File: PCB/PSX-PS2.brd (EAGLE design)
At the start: 58.5 x 61 mm, 15 parts

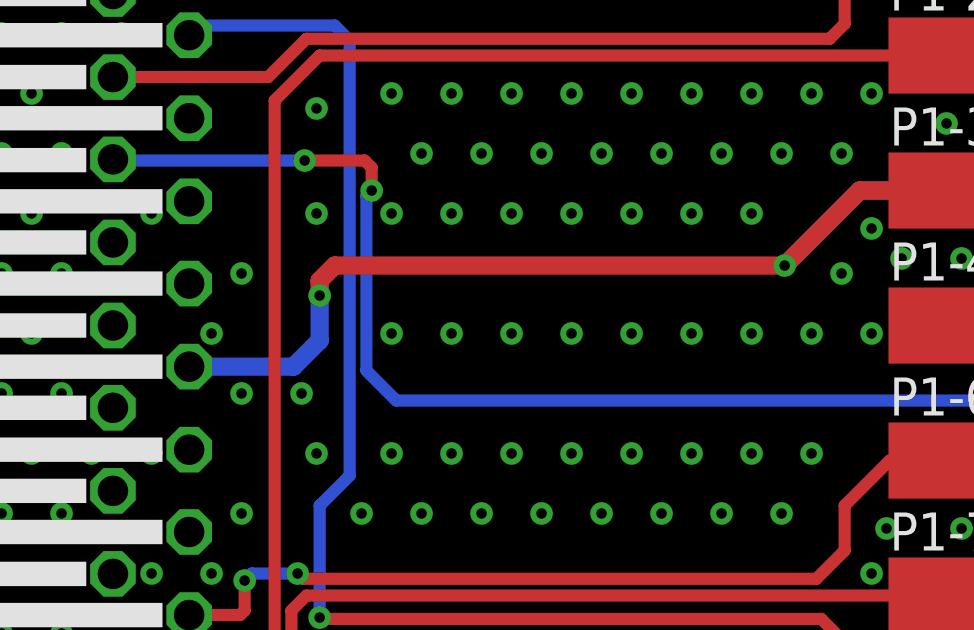
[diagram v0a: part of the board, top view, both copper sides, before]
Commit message: PS2 Power Pin Swap
The PCB could not detect the correct system using the 8V from the PS2 to the 5VIN on the ESP.  Moving to the 3V3 from the PS2 to 3V3IN on the ESP corrected the issue and the PCB not works as intended.
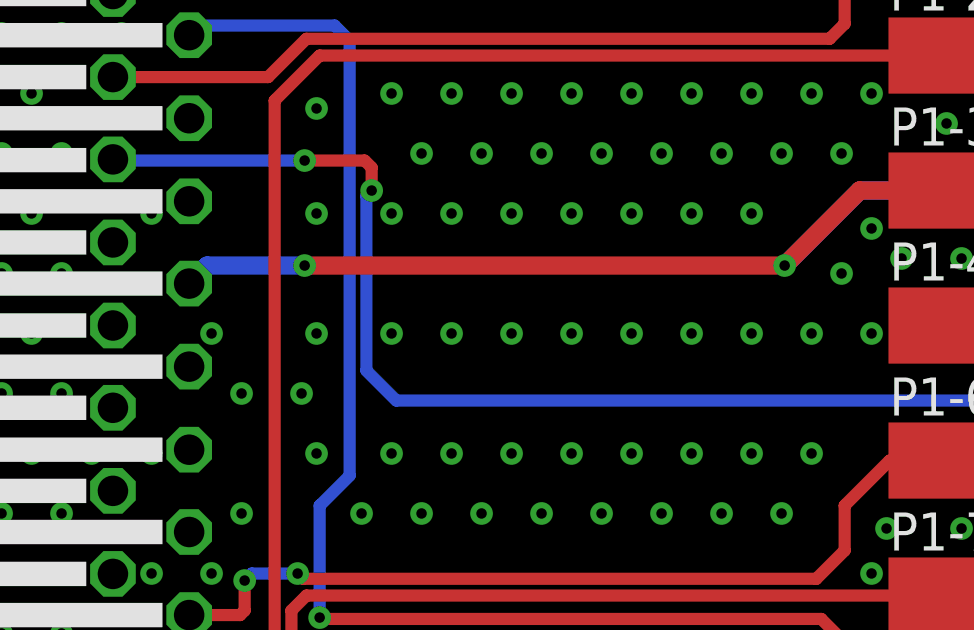
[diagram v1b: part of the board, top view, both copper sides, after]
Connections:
- removed net 5VIN: P1-3.1, P2-3.1, X1.7
- new net 3V3IN: P1-3.1, P2-3.1, X1.8
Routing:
- net 5VIN: track 42.5 -> 0.00 mm, vias 2 -> 0
- net 3V3IN: track 0.00 -> 40.2 mm, vias 0 -> 2
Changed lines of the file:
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@@
 <via x="14.8968" y="29.735840625" extent="1-16" drill="0.35"/>
 <via x="13.8968" y="31.735840625" extent="1-16" drill="0.35"/>
-<via x="14.8968" y="33.735840625" extent="1-16" drill="0.35"/>
+<via x="17.3968" y="31.735840625" extent="1-16" drill="0.35"/>
 <via x="14.8968" y="49.735840625" extent="1-16" drill="0.35"/>
 <via x="13.8968" y="51.735840625" extent="1-16" drill="0.35"/>
@@
 <via x="56.8968" y="45.735840625" extent="1-16" drill="0.35"/>
 </signal>
-<signal name="5VIN">
-<contactref element="X1" pad="7"/>
-<contactref element="P1-3" pad="1"/>
-<contactref element="P2-3" pad="1"/>
-<wire x1="13.15" y1="30.63" x2="16.63" y2="30.63" width="0.6096" layer="16"/>
-<wire x1="16.63" y1="30.63" x2="17.5" y2="31.5" width="0.6096" layer="16"/>
-<wire x1="17.5" y1="31.5" x2="17.5" y2="33" width="0.6096" layer="16"/>
-<via x="17.5" y="33" extent="1-16" drill="0.35"/>
-<wire x1="17.5" y1="33" x2="17.5" y2="33.5" width="0.6096" layer="1"/>
-<wire x1="17.5" y1="33.5" x2="18" y2="34" width="0.6096" layer="1"/>
-<wire x1="35.5" y1="36.5" x2="39" y2="36.5" width="0.6096" layer="1"/>
-<wire x1="18" y1="34" x2="33" y2="34" width="0.6096" layer="1"/>
-<wire x1="33" y1="34" x2="35.5" y2="36.5" width="0.6096" layer="1"/>
-<via x="33" y="34" extent="1-16" drill="0.35"/>
-<wire x1="33" y1="34" x2="35.5" y2="36.5" width="0.6096" layer="16"/>
-<wire x1="35.5" y1="36.5" x2="45" y2="36.5" width="0.6096" layer="16"/>
-</signal>
 <signal name="IO5">
 <contactref element="X1" pad="22"/>
@@
 <wire x1="34.5" y1="48.5" x2="42" y2="48.5" width="0.4064" layer="16"/>
 </signal>
+<signal name="3V3IN">
+<contactref element="X1" pad="8"/>
+<contactref element="P1-3" pad="1"/>
+<contactref element="P2-3" pad="1"/>
+<wire x1="35.5" y1="36.5" x2="39" y2="36.5" width="0.6096" layer="1"/>
+<wire x1="33" y1="34" x2="35.5" y2="36.5" width="0.6096" layer="1"/>
+<via x="33" y="34" extent="1-16" drill="0.35"/>
+<wire x1="33" y1="34" x2="35.5" y2="36.5" width="0.6096" layer="16"/>
+<wire x1="35.5" y1="36.5" x2="45" y2="36.5" width="0.6096" layer="16"/>
+<via x="17" y="34" extent="1-16" drill="0.35"/>
+<wire x1="13.7514" y1="34" x2="13.15" y2="33.3986" width="0.6096" layer="16"/>
+<wire x1="33" y1="34" x2="17" y2="34" width="0.6096" layer="1"/>
+<wire x1="17" y1="34" x2="13.7514" y2="34" width="0.6096" layer="16"/>
+</signal>
 </signals>

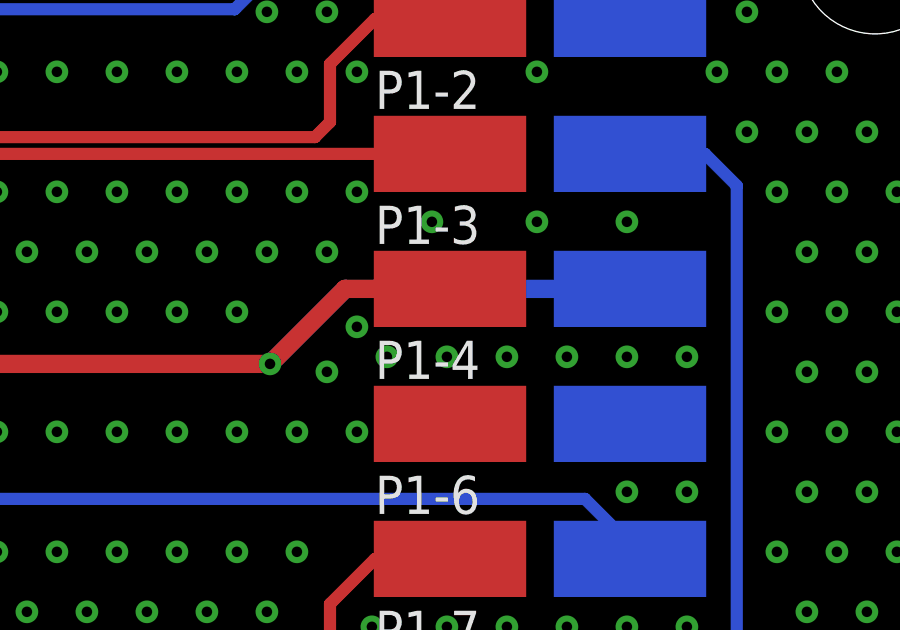
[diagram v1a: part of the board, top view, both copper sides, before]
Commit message: Updated Pad Name for 3V3 input
Pad name was still listed as P1-4/P2-4 which is the 8V pin, The pads have been renamed and order updated on the PCB
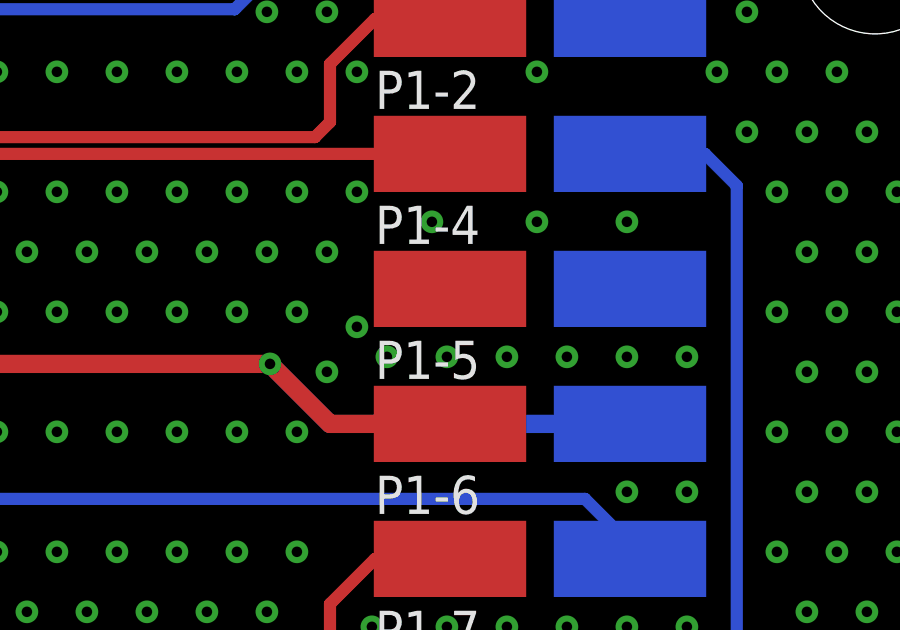
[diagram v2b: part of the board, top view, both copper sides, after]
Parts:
- removed P1-3, P2-3: (no value), wirepad:SMD2,54-5,08
- added P1-5, P2-5: (no value), wirepad:SMD2,54-5,08
- moved P1-4 4.50 mm to (39.0, 36.5)
- moved P2-4 4.50 mm to (45.0, 36.5)
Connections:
- net 3V3IN: now also P1-5.1, P2-5.1; no longer P1-3.1, P2-3.1
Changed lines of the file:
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@@
 <attribute name="VALUE" x="39" y="41" size="0.0254" layer="27" rot="R270"/>
 </element>
-<element name="P2-3" library="wirepad" library_urn="urn:adsk.eagle:library:412" package="SMD2,54-5,08" package3d_urn="urn:adsk.eagle:package:30841/1" value="" x="45" y="36.5" smashed="yes" rot="MR270">
-<attribute name="NAME" x="47.5" y="38" size="1.27" layer="26" rot="MR0"/>
-<attribute name="POPULARITY" value="21" x="74.21" y="-4.14" size="1.778" layer="28" rot="MR270" display="off"/>
-<attribute name="VALUE" x="45" y="36.5" size="0.0254" layer="28" rot="MR270"/>
+<element name="P2-5" library="wirepad" library_urn="urn:adsk.eagle:library:412" package="SMD2,54-5,08" package3d_urn="urn:adsk.eagle:package:30841/1" value="" x="45" y="32" smashed="yes" rot="MR270">
+<attribute name="NAME" x="47.5" y="33.5" size="1.27" layer="26" rot="MR0"/>
+<attribute name="POPULARITY" value="21" x="74.21" y="-8.64" size="1.778" layer="28" rot="MR270" display="off"/>
+<attribute name="VALUE" x="45" y="32" size="0.0254" layer="28" rot="MR270"/>
 </element>
 <element name="P1-9" library="wirepad" library_urn="urn:adsk.eagle:library:412" package="SMD2,54-5,08" package3d_urn="urn:adsk.eagle:package:30841/1" value="" x="39" y="18.5" smashed="yes" rot="R270">
@@
 <attribute name="VALUE" x="39" y="18.5" size="0.0254" layer="27" rot="R270"/>
 </element>
-<element name="P1-3" library="wirepad" library_urn="urn:adsk.eagle:library:412" package="SMD2,54-5,08" package3d_urn="urn:adsk.eagle:package:30841/1" value="" x="39" y="36.5" smashed="yes" rot="R270">
-<attribute name="NAME" x="36.5" y="38" size="1.27" layer="25"/>
-<attribute name="POPULARITY" value="21" x="9.79" y="11.1" size="1.778" layer="27" rot="R270" display="off"/>
-<attribute name="VALUE" x="39" y="36.5" size="0.0254" layer="27" rot="R270"/>
-</element>
-<element name="P2-4" library="wirepad" library_urn="urn:adsk.eagle:library:412" package="SMD2,54-5,08" package3d_urn="urn:adsk.eagle:package:30841/1" value="" x="45" y="32" smashed="yes" rot="MR270">
-<attribute name="NAME" x="47.5" y="33.5" size="1.27" layer="26" rot="MR0"/>
-<attribute name="POPULARITY" value="21" x="74.21" y="-13.72" size="1.778" layer="28" rot="MR270" display="off"/>
-<attribute name="VALUE" x="45" y="32" size="0.0254" layer="28" rot="MR270"/>
+<element name="P1-5" library="wirepad" library_urn="urn:adsk.eagle:library:412" package="SMD2,54-5,08" package3d_urn="urn:adsk.eagle:package:30841/1" value="" x="39" y="32" smashed="yes" rot="R270">
+<attribute name="NAME" x="36.5" y="33.5" size="1.27" layer="25"/>
+<attribute name="POPULARITY" value="21" x="9.79" y="6.6" size="1.778" layer="27" rot="R270" display="off"/>
+<attribute name="VALUE" x="39" y="32" size="0.0254" layer="27" rot="R270"/>
+</element>
+<element name="P2-4" library="wirepad" library_urn="urn:adsk.eagle:library:412" package="SMD2,54-5,08" package3d_urn="urn:adsk.eagle:package:30841/1" value="" x="45" y="36.5" smashed="yes" rot="MR270">
+<attribute name="NAME" x="47.5" y="38" size="1.27" layer="26" rot="MR0"/>
+<attribute name="POPULARITY" value="21" x="74.21" y="-9.22" size="1.778" layer="28" rot="MR270" display="off"/>
+<attribute name="VALUE" x="45" y="36.5" size="0.0254" layer="28" rot="MR270"/>
 </element>
 <element name="P2-1" library="wirepad" library_urn="urn:adsk.eagle:library:412" package="SMD2,54-5,08" package3d_urn="urn:adsk.eagle:package:30841/1" value="" x="45" y="45.5" smashed="yes" rot="MR270">
@@
 <attribute name="VALUE" x="45" y="45.5" size="0.0254" layer="28" rot="MR270"/>
 </element>
-<element name="P1-4" library="wirepad" library_urn="urn:adsk.eagle:library:412" package="SMD2,54-5,08" package3d_urn="urn:adsk.eagle:package:30841/1" value="" x="39" y="32" smashed="yes" rot="R270">
-<attribute name="NAME" x="36.5" y="33.5" size="1.27" layer="25"/>
-<attribute name="POPULARITY" value="21" x="9.79" y="1.52" size="1.778" layer="27" rot="R270" display="off"/>
-<attribute name="VALUE" x="39" y="32" size="0.0254" layer="27" rot="R270"/>
+<element name="P1-4" library="wirepad" library_urn="urn:adsk.eagle:library:412" package="SMD2,54-5,08" package3d_urn="urn:adsk.eagle:package:30841/1" value="" x="39" y="36.5" smashed="yes" rot="R270">
+<attribute name="NAME" x="36.5" y="38" size="1.27" layer="25"/>
+<attribute name="POPULARITY" value="21" x="9.79" y="6.02" size="1.778" layer="27" rot="R270" display="off"/>
+<attribute name="VALUE" x="39" y="36.5" size="0.0254" layer="27" rot="R270"/>
 </element>
 <element name="P2-6" library="wirepad" library_urn="urn:adsk.eagle:library:412" package="SMD2,54-5,08" package3d_urn="urn:adsk.eagle:package:30841/1" value="" x="45" y="27.5" smashed="yes" rot="MR270">
@@
 <via x="35.8968" y="23.735840625" extent="1-16" drill="0.35"/>
 <via x="36.3968" y="25.235840625" extent="1-16" drill="0.35"/>
-<via x="35.8968" y="31.735840625" extent="1-16" drill="0.35"/>
+<via x="33.8968" y="35.735840625" extent="1-16" drill="0.35"/>
 <via x="36.8968" y="34.235840625" extent="1-16" drill="0.35"/>
 <via x="35.8968" y="35.235840625" extent="1-16" drill="0.35"/>
@@
 <signal name="3V3IN">
 <contactref element="X1" pad="8"/>
-<contactref element="P1-3" pad="1"/>
-<contactref element="P2-3" pad="1"/>
-<wire x1="35.5" y1="36.5" x2="39" y2="36.5" width="0.6096" layer="1"/>
-<wire x1="33" y1="34" x2="35.5" y2="36.5" width="0.6096" layer="1"/>
+<contactref element="P1-5" pad="1"/>
+<contactref element="P2-5" pad="1"/>
+<wire x1="39" y1="32" x2="35" y2="32" width="0.6096" layer="1"/>
+<wire x1="33" y1="34" x2="35" y2="32" width="0.6096" layer="1"/>
 <via x="33" y="34" extent="1-16" drill="0.35"/>
-<wire x1="33" y1="34" x2="35.5" y2="36.5" width="0.6096" layer="16"/>
-<wire x1="35.5" y1="36.5" x2="45" y2="36.5" width="0.6096" layer="16"/>
+<wire x1="45" y1="32" x2="35" y2="32" width="0.6096" layer="16"/>
+<wire x1="33" y1="34" x2="35" y2="32" width="0.6096" layer="16"/>
 <via x="17" y="34" extent="1-16" drill="0.35"/>
 <wire x1="13.7514" y1="34" x2="13.15" y2="33.3986" width="0.6096" layer="16"/>

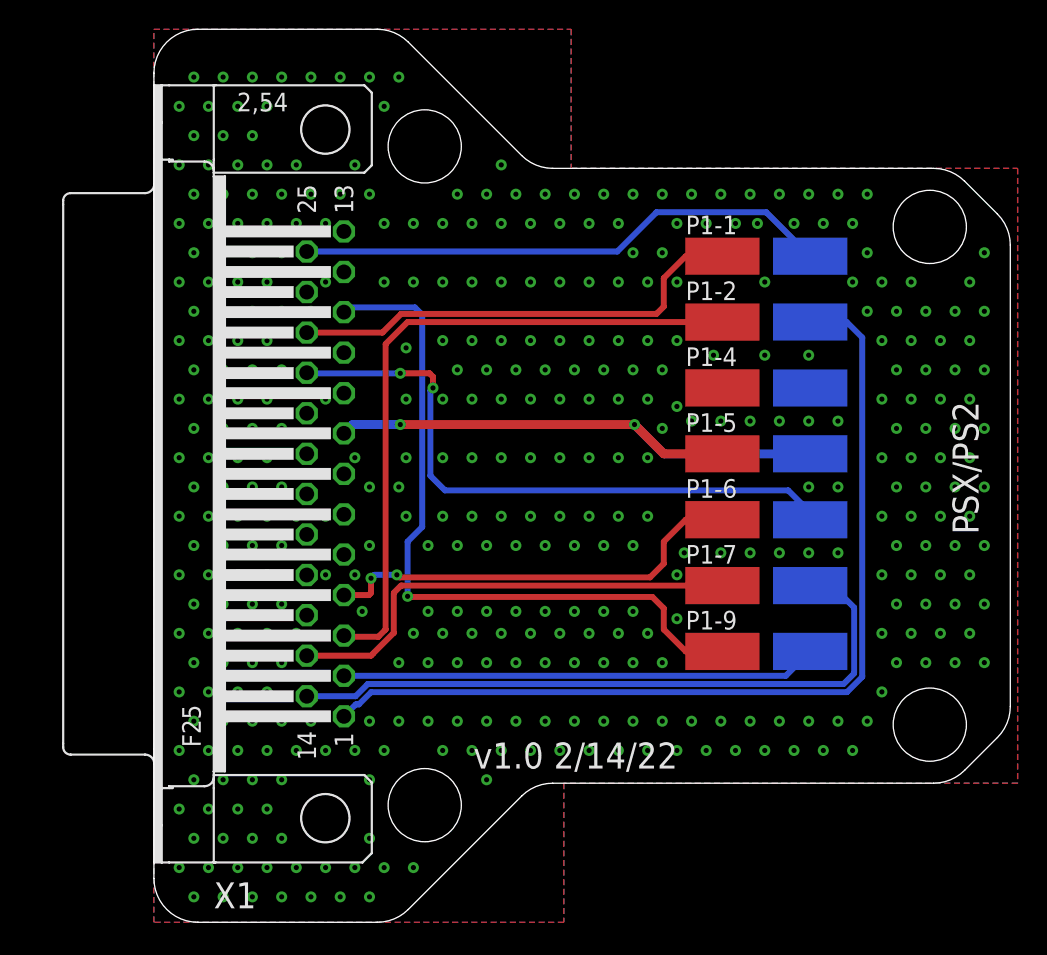
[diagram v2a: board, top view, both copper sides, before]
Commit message: Power Pin addition
After working with Darthcloud, it was revealed that some PS2 consoles have weak VIN on either the 8V or the 3V3.  To make sure this PCB will work in either situation, I have added the 8V (Pad 3) pad back on to the PCB in addition to the 3V3 Pad (Pad 5).  Only one needs to be used to power the ESP.
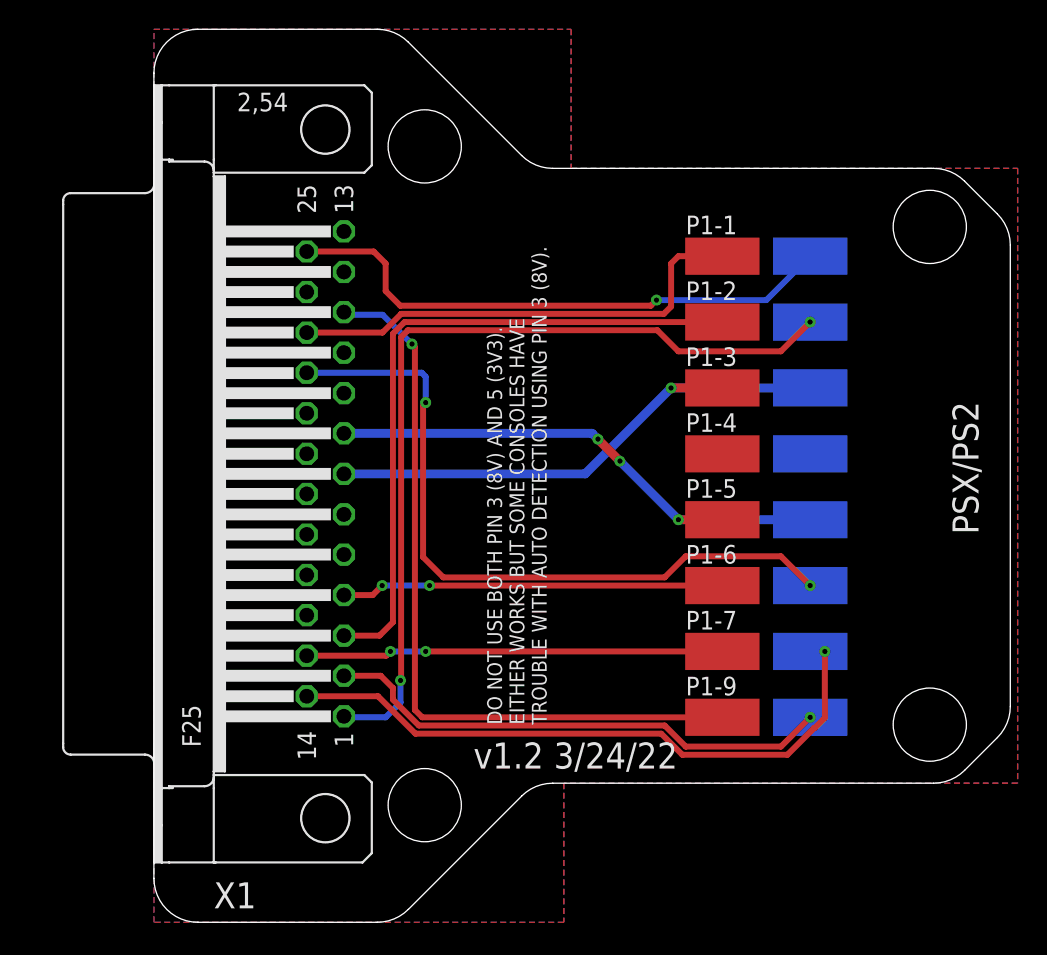
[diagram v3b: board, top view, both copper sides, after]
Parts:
- added P1-3, P2-3: (no value), wirepad:SMD2,54-5,08
- moved P1-4 4.50 mm to (39.0, 32.0)
- moved P1-5 4.50 mm to (39.0, 27.5)
- moved P1-6 4.50 mm to (39.0, 23.0)
- moved P1-7 4.50 mm to (39.0, 18.5)
- moved P1-9 4.50 mm to (39.0, 14.0)
- moved P2-4 4.50 mm to (45.0, 32.0)
- moved P2-5 4.50 mm to (45.0, 27.5)
- moved P2-6 4.50 mm to (45.0, 23.0)
- moved P2-7 4.50 mm to (45.0, 18.5)
- moved P2-9 4.50 mm to (45.0, 14.0)
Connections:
- new net VIN: P1-3.1, P2-3.1, X1.7
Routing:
- net VIN: track 0.00 -> 37.8 mm, vias 0 -> 1
- net IO5: track 43.1 -> 49.1 mm
- net IO27: track 63.7 -> 58.9 mm, vias 0 -> 2
- net IO34: track 29.6 -> 26.1 mm
- net IO33: track 32.0 -> 28.5 mm, vias 0 -> 2
- net IO25: track 32.5 -> 35.1 mm, vias 0 -> 1
- net IO21: track 49.2 -> 51.8 mm
- net IO26: track 46.2 -> 43.6 mm, vias 0 -> 1
- net 3V3IN: track 39.8 -> 37.3 mm, vias 2 -> 3
- net IO22: track 36.7 -> 38.4 mm, vias 0 -> 1
- net IO19: track 31.7 -> 32.3 mm
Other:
- board text added: "DO NOT USE BOTH PIN 3 (8V) AND 5 (3V3). EITHER WORKS BUT SOME CONSOLES HAVE TROUBLE WITH AUTO DETECTION USING PIN 3 (8V)."
- board text added: "v1.2 3/24/22"
- board text removed: "v1.0 2/14/22"
